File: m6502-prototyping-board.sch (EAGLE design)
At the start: 31 parts

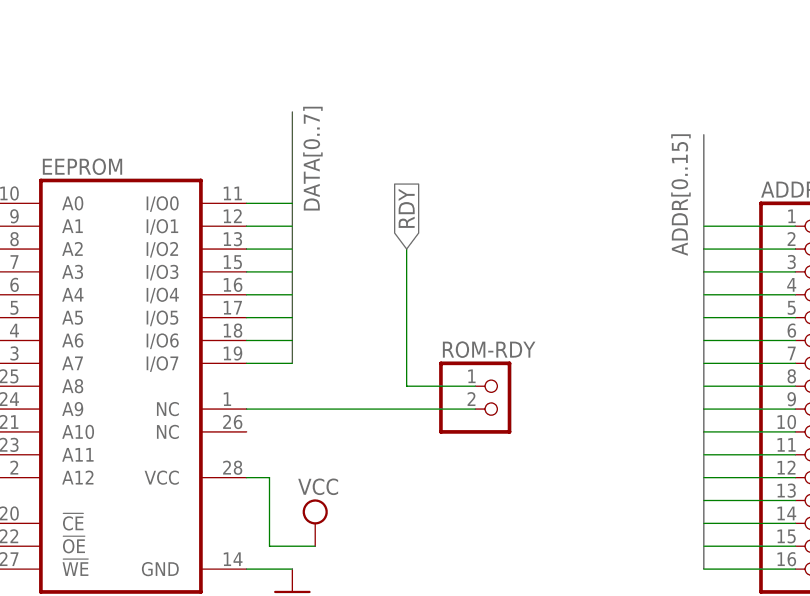
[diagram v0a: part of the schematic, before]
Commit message: removed RDY connection to eeprom
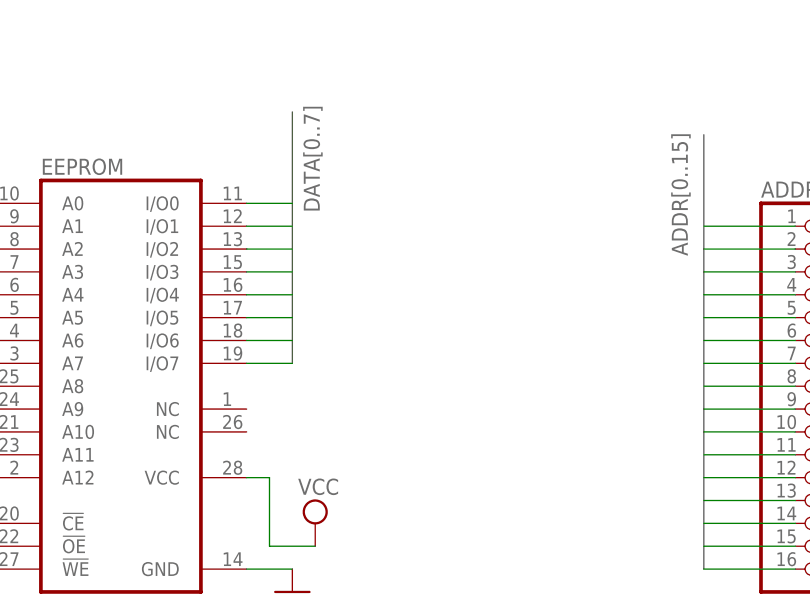
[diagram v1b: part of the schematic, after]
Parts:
- removed ROM-RDY: (no value), pinhead:PINHD-1X2
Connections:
- removed net N$8: EEPROM.NC, ROM-RDY.2
- net RDY: no longer ROM-RDY.1
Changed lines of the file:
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@@
 <part name="IRQ" library="pinhead" library_urn="urn:adsk.eagle:library:325" deviceset="PINHD-1X2" device="" package3d_urn="urn:adsk.eagle:package:22435/2"/>
 <part name="RDY" library="pinhead" library_urn="urn:adsk.eagle:library:325" deviceset="PINHD-1X2" device="" package3d_urn="urn:adsk.eagle:package:22435/2"/>
-<part name="ROM-RDY" library="pinhead" library_urn="urn:adsk.eagle:library:325" deviceset="PINHD-1X2" device="" package3d_urn="urn:adsk.eagle:package:22435/2"/>
 <part name="QG1" library="crystal" library_urn="urn:adsk.eagle:library:204" deviceset="XO-" device="14" package3d_urn="urn:adsk.eagle:package:12068/1"/>
 <part name="CLK-CTL" library="pinhead" library_urn="urn:adsk.eagle:library:325" deviceset="PINHD-1X2" device="" package3d_urn="urn:adsk.eagle:package:22435/2"/>
@@
 <attribute name="NAME" x="13.97" y="132.715" size="1.778" layer="95"/>
 <attribute name="VALUE" x="13.97" y="121.92" size="1.778" layer="96"/>
-</instance>
-<instance part="ROM-RDY" gate="G$1" x="213.36" y="68.58" smashed="yes">
-<attribute name="NAME" x="207.01" y="74.295" size="1.778" layer="95"/>
-<attribute name="VALUE" x="207.01" y="63.5" size="1.778" layer="96"/>
 </instance>
 <instance part="QG1" gate="G$1" x="58.42" y="144.78" smashed="yes">
@@
 <pinref part="SIG" gate="A" pin="1"/>
 </segment>
-<segment>
-<pinref part="ROM-RDY" gate="G$1" pin="1"/>
-<wire x1="210.82" y1="71.12" x2="203.2" y2="71.12" width="0.1524" layer="91"/>
-<wire x1="203.2" y1="71.12" x2="203.2" y2="86.36" width="0.1524" layer="91"/>
-<label x="203.2" y="86.36" size="1.778" layer="95" rot="R90" xref="yes"/>
-</segment>
 </net>
 <net name="N$3" class="0">
@@
 </segment>
 </net>
-<net name="N$8" class="0">
-<segment>
-<pinref part="EEPROM" gate="G$1" pin="NC"/>
-<pinref part="ROM-RDY" gate="G$1" pin="2"/>
-<wire x1="185.42" y1="68.58" x2="210.82" y2="68.58" width="0.1524" layer="91"/>
-</segment>
-</net>
